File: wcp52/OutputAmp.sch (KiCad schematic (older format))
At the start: 33 parts, among them Q4 MMBT3906, Q5 2N7002, Q6 2N7002, U6 AD8000YRDZ, U7 THS3001IDGN, U8 MAADSS0008

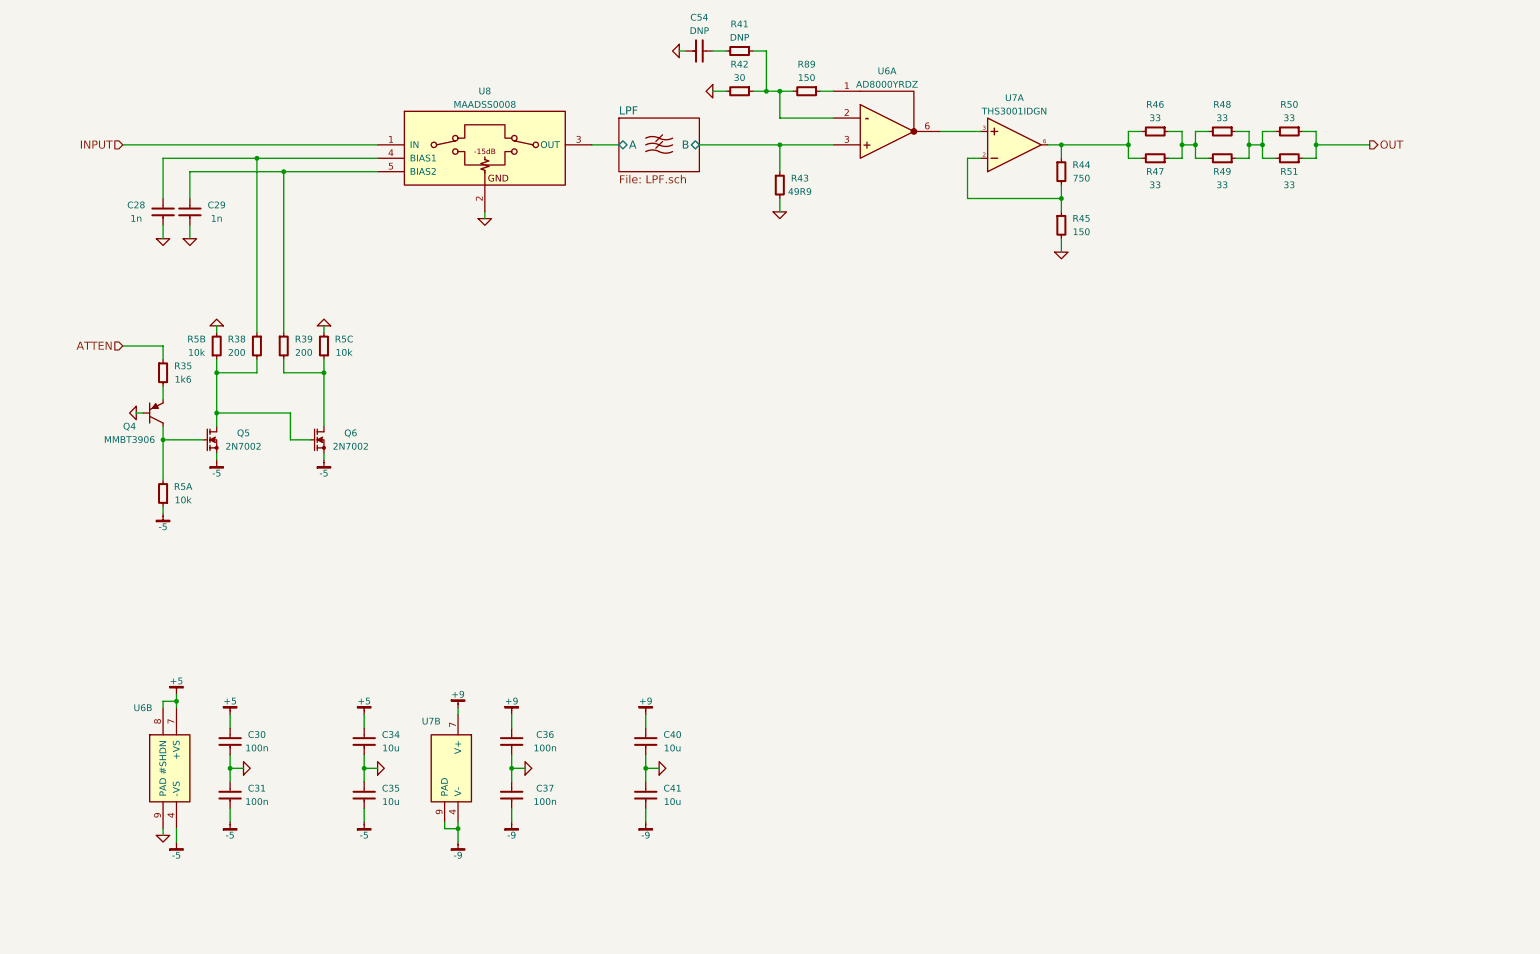
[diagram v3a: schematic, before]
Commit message: Reannotate parts. May need to tweak silkscreen
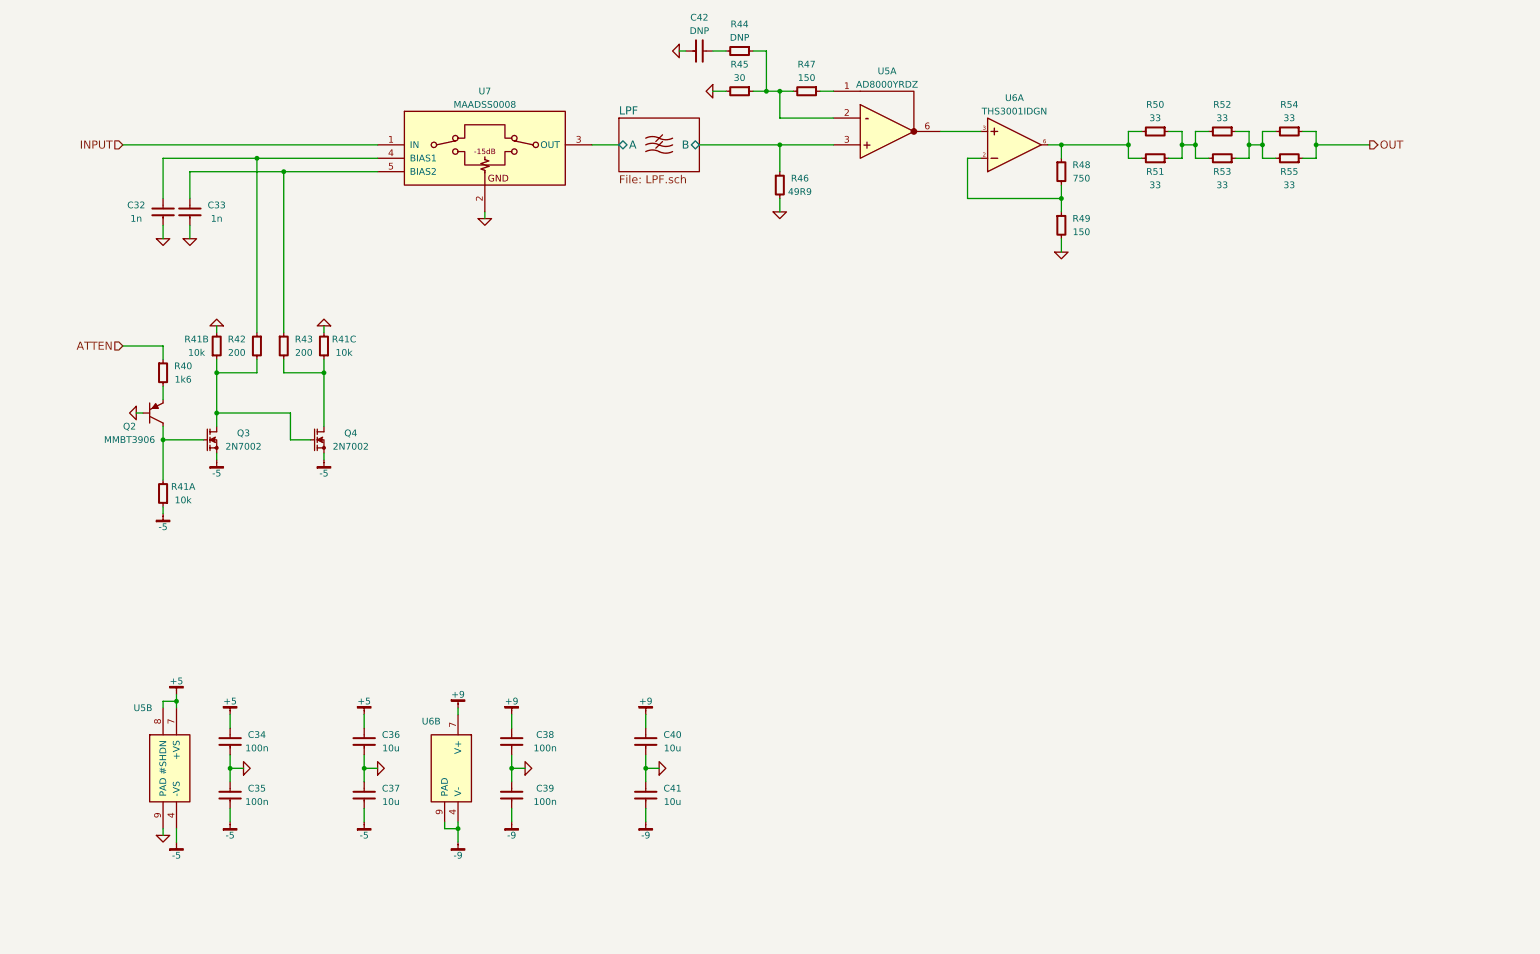
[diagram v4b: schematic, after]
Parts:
- C32: renamed from C28; OldReference (none) -> C28
- C33: renamed from C29; OldReference (none) -> C29
- C34: renamed from C30; OldReference (none) -> C30
- C35: renamed from C31; OldReference (none) -> C31
- C36: renamed from C34; OldReference (none) -> C34
- C37: renamed from C35; OldReference (none) -> C35
- C38: renamed from C36; OldReference (none) -> C36
- C39: renamed from C37; OldReference (none) -> C37
- C40: OldReference (none) -> C40
- C41: OldReference (none) -> C41
- C42: renamed from C54; OldReference (none) -> C54
- Q2: renamed from Q4; OldReference (none) -> Q4
- Q3: renamed from Q5; OldReference (none) -> Q5
- Q4: renamed from Q6; OldReference (none) -> Q6
- R40: renamed from R35; OldReference (none) -> R35
- R41: renamed from R5; OldReference (none) -> R5
- R42: renamed from R38; OldReference (none) -> R38
- R43: renamed from R39; OldReference (none) -> R39
- R44: renamed from R41; OldReference (none) -> R41
- R45: renamed from R42; OldReference (none) -> R42
- R46: renamed from R43; OldReference (none) -> R43
- R47: renamed from R89; OldReference (none) -> R89
- R48: renamed from R44; OldReference (none) -> R44
- R49: renamed from R45; OldReference (none) -> R45
- R50: renamed from R46; OldReference (none) -> R46
- R51: renamed from R47; OldReference (none) -> R47
- R52: renamed from R48; OldReference (none) -> R48
- R53: renamed from R49; OldReference (none) -> R49
- R54: renamed from R50; OldReference (none) -> R50
- R55: renamed from R51; OldReference (none) -> R51
- U5: renamed from U6; OldReference (none) -> U6
- U6: renamed from U7; OldReference (none) -> U7
- U7: renamed from U8; OldReference (none) -> U8

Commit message: Schematic touchups
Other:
- note added: "@C42 and @R44 are optional compensation devices to boost\ngain slightly at high frequency, if post-fab testing shows that\nstray capacitance from layout results in a rolloff. In the first\nrevision, do not populate them."
- note added: "@U5: 15dB gain"
- note added: "@U6: 15dB gain"
- moved on the sheet: C32, C33, C42, Q2, Q3, Q4, R40, R41A, R41B, R41C, R42, R43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

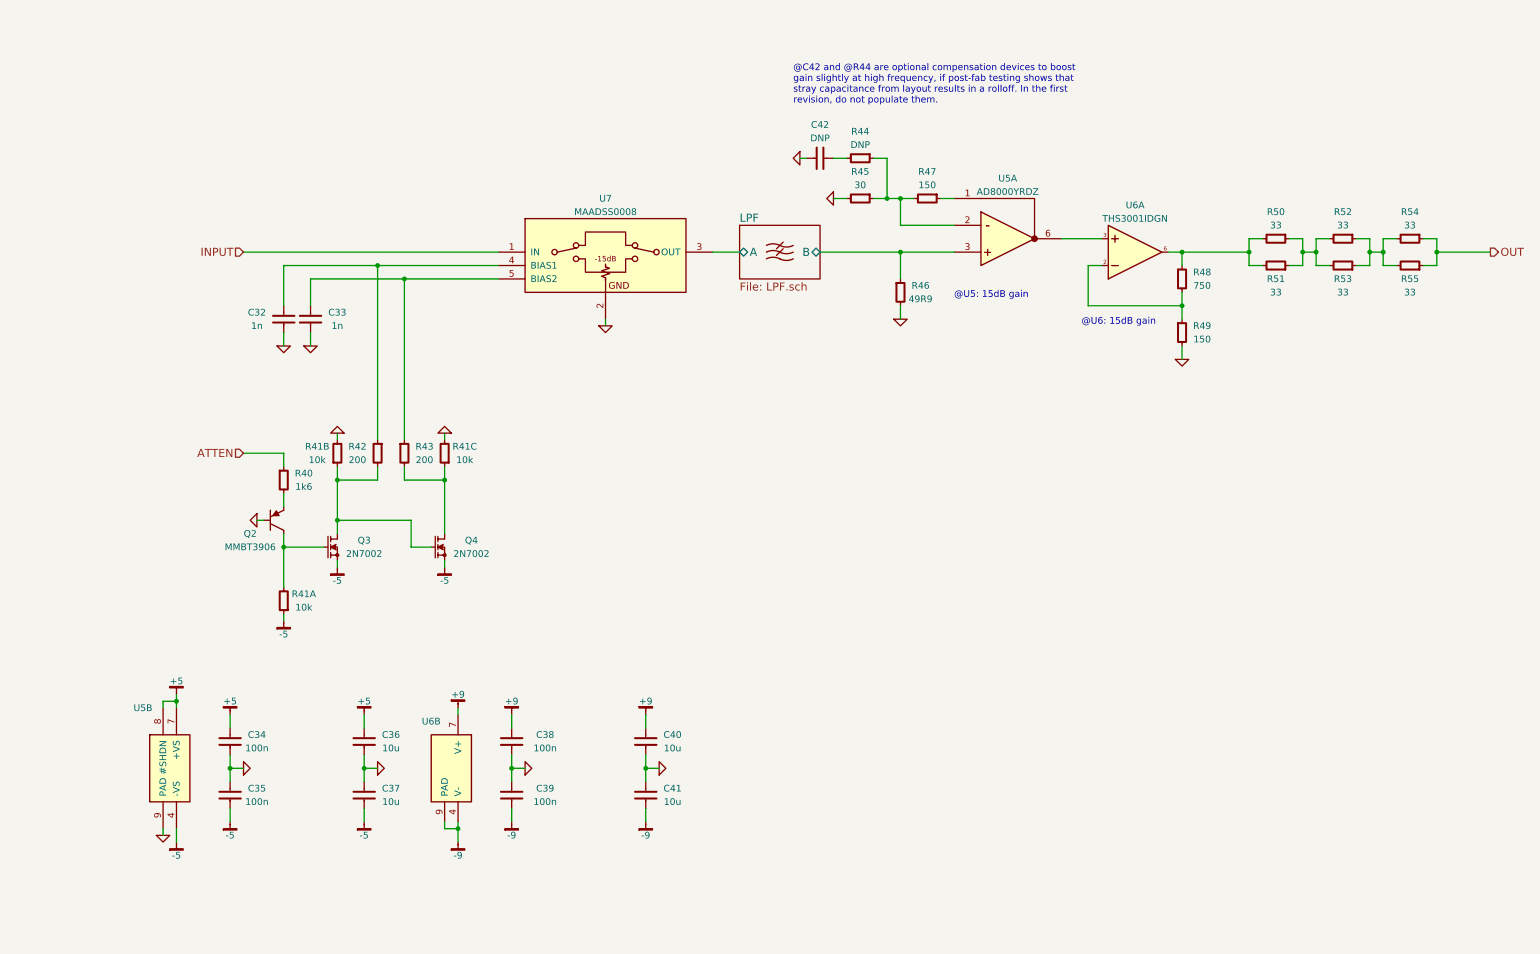
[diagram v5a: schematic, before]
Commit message: Change schematic pages to letter size
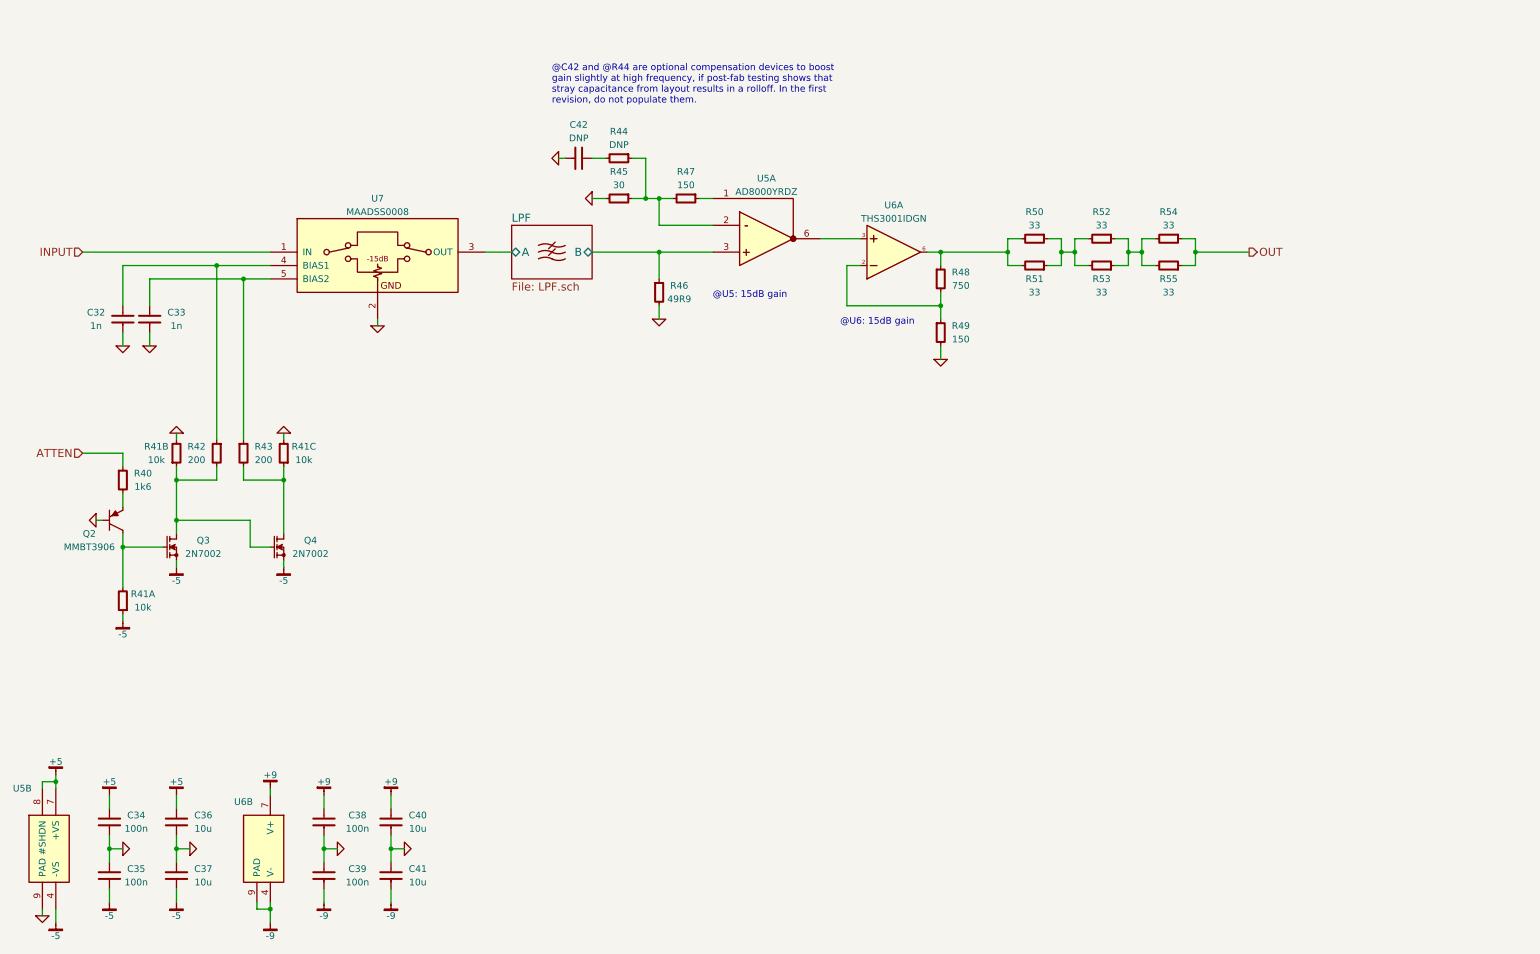
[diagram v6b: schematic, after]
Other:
- moved on the sheet: C32, C33, C34, C35, C36, C37, C38, C39, C40, C41, C42, Q2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

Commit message: BOM fixes
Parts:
- U7: BOM DIST DIGIKEY 1465-1252-1-ND -> IC MACOM MAADSS0008
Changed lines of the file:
@@
 EESchema Schematic File Version 2
-LIBS:Altera
-LIBS:AnalogDevices
-LIBS:Atmel
-LIBS:conn-2mm
-LIBS:conn-100mil
-LIBS:conn-cui
-LIBS:conn-fci
-LIBS:conn-linx
-LIBS:conn-molex
-LIBS:conn-tagconnect
-LIBS:conn-test
-LIBS:DiodesInc
-LIBS:display
-LIBS:_electromech
-LIBS:Fairchild
-LIBS:FTDI
-LIBS:Intersil
-LIBS:Lattice
-LIBS:_linear
-LIBS:LinearTech
-LIBS:Littelfuse
-LIBS:logic-4000
-LIBS:logic-7400
-LIBS:MACOM
-LIBS:maxim
-LIBS:mechanical
-LIBS:Microchip
-LIBS:Micron
-LIBS:NXP
-LIBS:onsemi
-LIBS:passive
-LIBS:pasv-BiTech
-LIBS:pasv-Bourns
-LIBS:pasv-cap
-LIBS:pasv-ind
-LIBS:pasv-res
-LIBS:pcb
-LIBS:power
-LIBS:_semi
-LIBS:semi-diode-1N
-LIBS:semi-diode-BA
-LIBS:semi-diode-MCC
-LIBS:semi-diode-MMB
-LIBS:semi-diode-NXP
-LIBS:semi-diode-OnSemi
-LIBS:semi-diode-Vishay
-LIBS:semi-opto-misc
-LIBS:semi-thyristor-2N
-LIBS:semi-trans-2N
-LIBS:semi-trans-AO
-LIBS:semi-trans-BC
-LIBS:semi-trans-DiodesInc
-LIBS:semi-trans-Fairchild
-LIBS:semi-trans-Infineon
-LIBS:semi-trans-IntRect
-LIBS:semi-trans-IXYS
-LIBS:semi-trans-misc
-LIBS:semi-trans-MMB
-LIBS:semi-trans-MPS
-LIBS:semi-trans-NXP
-LIBS:semi-trans-PZT
-LIBS:semi-trans-TI
-LIBS:semi-trans-TIP
-LIBS:semi-trans-Toshiba
-LIBS:silabs
-LIBS:skyworks
-LIBS:ST
-LIBS:st_ic
-LIBS:st_semi
-LIBS:supertex
-LIBS:symbol
-LIBS:TexasInstruments
-LIBS:vishay_semi
-LIBS:Xilinx
-LIBS:pasv-xtal
-LIBS:conn-te
 LIBS:wcp52-cache
 EELAYER 25 0
@@
 F 3 "" H 3100 2800 60  0000 C CNN
 F 4 "Value" H 3400 2800 60  0001 C CNN "Manuf"
-F 5 "DIST DIGIKEY 1465-1252-1-ND" H 3900 3700 60  0001 C CNN "BOM"
+F 5 "IC MACOM MAADSS0008" H 3900 3700 60  0001 C CNN "BOM"
 F 6 "U8" H 3400 2800 50  0001 C CNN "OldReference"
 	1    3400 2800

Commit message: Prepare to fab
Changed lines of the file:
@@
 $EndComp
 Wire Wire Line
-	5000 2800 5500 2800
-Wire Wire Line
-	5500 2800 5900 2800
+	5000 2800 5900 2800
 Wire Wire Line
 	5800 2400 5900 2400
 Wire Wire Line
-	5300 2400 5400 2400
-Wire Wire Line
-	5400 2400 5500 2400
-Wire Wire Line
-	5500 2400 5600 2400
+	5300 2400 5600 2400
 Wire Wire Line
 	5500 2400 5500 2600
@@
 	7000 2700 6700 2700
 Wire Wire Line
-	7600 3100 7600 3200
-Wire Wire Line
-	7600 3200 7600 3300
+	7600 3100 7600 3300
 Wire Wire Line
 	7600 3200 6900 3200
@@
 Connection ~ 7600 3200
 Wire Wire Line
-	7500 2800 7600 2800
-Wire Wire Line
-	7600 2800 8100 2800
+	7500 2800 8100 2800
 Wire Wire Line
 	7600 2800 7600 2900
@@
 	8500 2900 8400 2900
 Wire Wire Line
-	8500 2700 8500 2800
-Wire Wire Line
-	8500 2800 8500 2900
+	8500 2700 8500 2900
 Wire Wire Line
 	8500 2700 8400 2700
@@
 	8200 2700 8100 2700
 Wire Wire Line
-	8100 2700 8100 2800
-Wire Wire Line
-	8100 2800 8100 2900
+	8100 2700 8100 2900
 Wire Wire Line
 	8100 2900 8200 2900
@@
 	9000 2900 8900 2900
 Wire Wire Line
-	9000 2700 9000 2800
-Wire Wire Line
-	9000 2800 9000 2900
+	9000 2700 9000 2900
 Wire Wire Line
 	9000 2700 8900 2700
@@
 	8700 2700 8600 2700
 Wire Wire Line
-	8600 2700 8600 2800
-Wire Wire Line
-	8600 2800 8600 2900
+	8600 2700 8600 2900
 Wire Wire Line
 	8600 2900 8700 2900
@@
 	9500 2900 9400 2900
 Wire Wire Line
-	9500 2700 9500 2800
-Wire Wire Line
-	9500 2800 9500 2900
+	9500 2700 9500 2900
 Wire Wire Line
 	9500 2700 9400 2700
@@
 	9200 2700 9100 2700
 Wire Wire Line
-	9100 2700 9100 2800
-Wire Wire Line
-	9100 2800 9100 2900
+	9100 2700 9100 2900
 Wire Wire Line
 	9100 2900 9200 2900
@@
 $EndComp
 Wire Wire Line
-	1000 6700 1000 6750
-Wire Wire Line
-	1000 6750 1000 6800
+	1000 6700 1000 6800
 Wire Wire Line
 	1000 6750 900  6750
@@
 	1400 6850 1400 6950
 Wire Wire Line
-	1400 7150 1400 7250
-Wire Wire Line
-	1400 7250 1400 7350
+	1400 7150 1400 7350
 $Comp
 L C-0805 C36
@@
 $EndComp
 Wire Wire Line
-	1900 7150 1900 7250
-Wire Wire Line
-	1900 7250 1900 7350
+	1900 7150 1900 7350
 $Comp
 L GND #PWR0134
@@
 $EndComp
 Wire Wire Line
-	2600 7650 2600 7700
-Wire Wire Line
-	2600 7700 2600 7800
+	2600 7650 2600 7800
 Wire Wire Line
 	2600 7700 2500 7700
@@
 	3000 6850 3000 6950
 Wire Wire Line
-	3000 7150 3000 7250
-Wire Wire Line
-	3000 7250 3000 7350
-Wire Wire Line
-	3500 7150 3500 7250
-Wire Wire Line
-	3500 7250 3500 7350
+	3000 7150 3000 7350
+Wire Wire Line
+	3500 7150 3500 7350
 $Comp
 L GND #PWR0141
@@
 	2200 4200 2200 2900
 Wire Wire Line
-	1500 2900 2200 2900
-Wire Wire Line
-	2200 2900 2600 2900
-Wire Wire Line
-	1700 3000 2400 3000
-Wire Wire Line
-	2400 3000 2600 3000
+	1500 2900 2600 2900
+Wire Wire Line
+	1700 3000 2600 3000
 Wire Wire Line
 	2400 3000 2400 4200
@@
 	2200 4500 1900 4500
 Wire Wire Line
-	1900 4400 1900 4500
-Wire Wire Line
-	1900 4500 1900 4800
-Wire Wire Line
-	1900 4800 1900 4900
+	1900 4400 1900 4900
 Wire Wire Line
 	2400 4400 2400 4500
@@
 	2400 4500 2700 4500
 Wire Wire Line
-	2700 4400 2700 4500
-Wire Wire Line
-	2700 4500 2700 4900
+	2700 4400 2700 4900
 $Comp
 L 2N7002 Q3
@@
 	1500 5550 1500 5500
 Wire Wire Line
-	1500 4900 1500 5000
-Wire Wire Line
-	1500 5000 1500 5300
+	1500 4900 1500 5300
 Wire Wire Line
 	1500 5000 1800 5000
